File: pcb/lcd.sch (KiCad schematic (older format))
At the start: 1 part, among them J4 ITDB_TFT

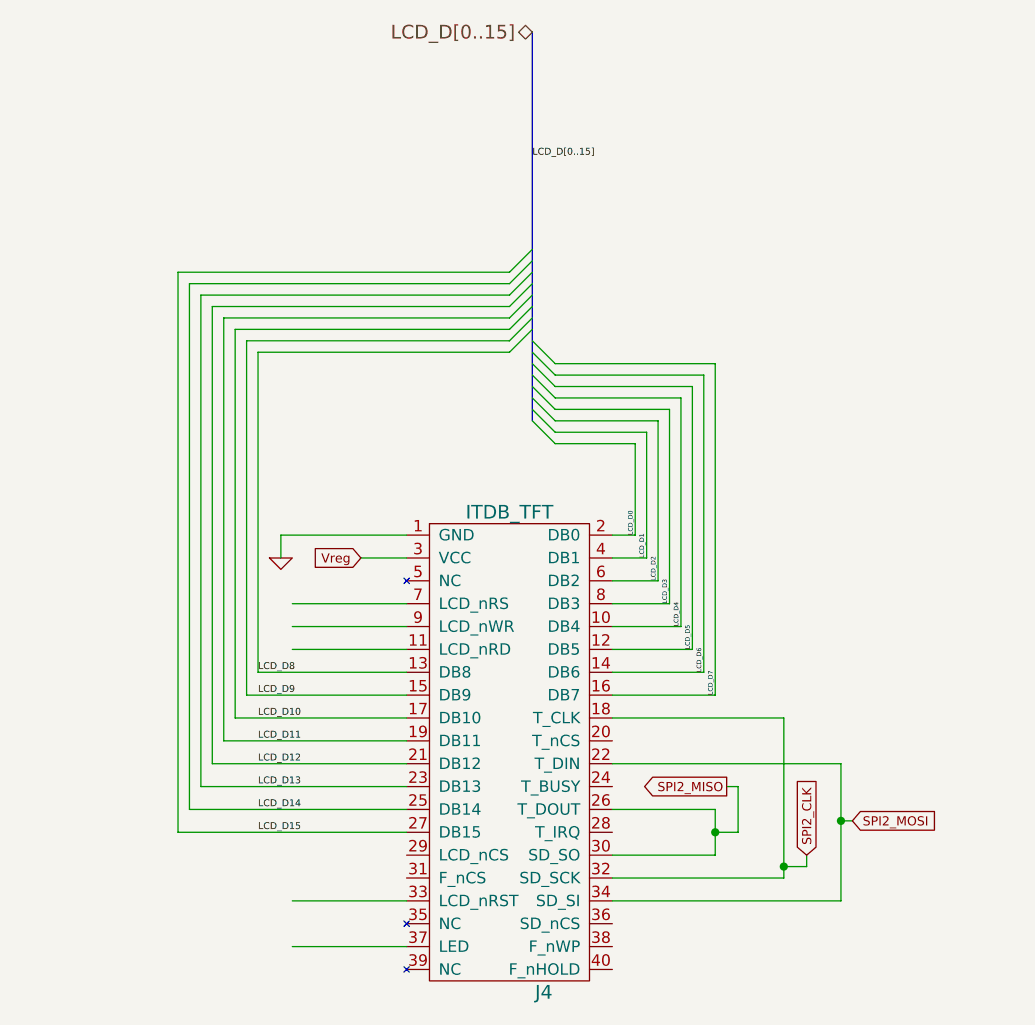
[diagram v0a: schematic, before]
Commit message: A few things: Remapped all interrupts and identified unusable pins on board Added all required connections for LCD and company Added pull-down resistor on STM32W Renamed some internal signals on RF for consistency
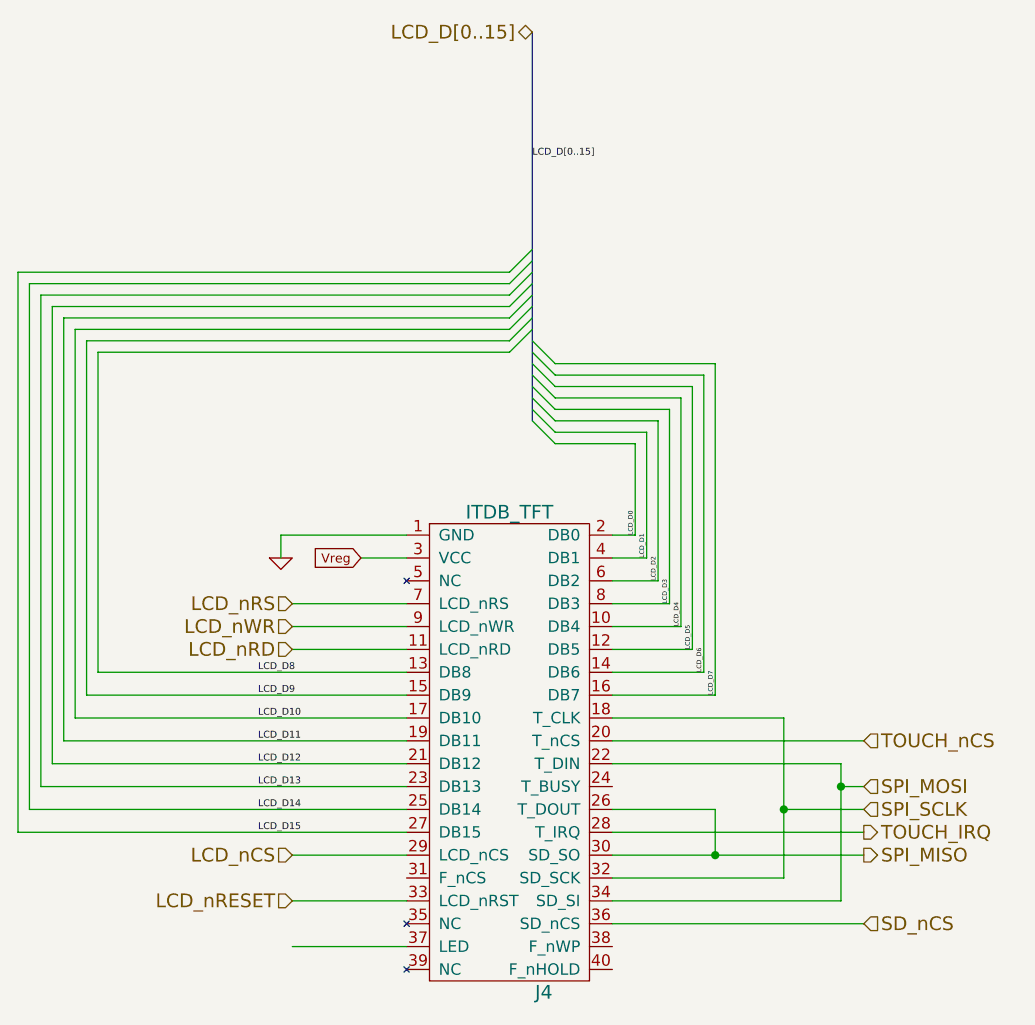
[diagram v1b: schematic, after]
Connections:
- net labels added: LCD_nCS, LCD_nRD, LCD_nRESET, LCD_nRS, LCD_nWR, SD_nCS, SPI_MISO, SPI_MOSI, SPI_SCLK, TOUCH_IRQ, TOUCH_nCS
- net labels removed: SPI2_CLK, SPI2_MISO, SPI2_MOSI
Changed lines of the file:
@@
-EESchema Schematic File Version 2  date 10/11/2012 11:52:24 AM
+EESchema Schematic File Version 2  date Sat 27 Oct 2012 09:22:30 PM EDT
 LIBS:power
 LIBS:device
@@
 $Descr A4 11700 8267
 encoding utf-8
-Sheet 5 7
+Sheet 2 7
 Title ""
-Date "11 oct 2012"
+Date "28 oct 2012"
 Rev ""
 Comp ""
@@
 Comment4 ""
 $EndDescr
+Wire Wire Line
+	6400 5100 5300 5100
+Wire Wire Line
+	6400 4700 5300 4700
+Wire Wire Line
+	6400 4600 6050 4600
+Wire Wire Line
+	4400 4800 3900 4800
+Wire Wire Line
+	4400 4300 2900 4300
+Wire Wire Line
+	4200 3500 4400 3500
+Wire Wire Line
+	3850 3500 3850 3400
+Wire Wire Line
+	3850 3400 4400 3400
+Wire Wire Line
+	5300 4400 6300 4400
+Wire Wire Line
+	5300 4600 5750 4600
+Wire Wire Line
+	5300 4200 6050 4200
+Wire Wire Line
+	5300 5000 6300 5000
+Wire Wire Line
+	5300 4900 6050 4900
+Wire Wire Line
+	4400 5000 3900 5000
+Wire Wire Line
+	4400 5200 3900 5200
+Wire Wire Line
+	4400 3900 3900 3900
+Wire Wire Line
+	4400 3800 3900 3800
+Wire Wire Line
+	4400 3700 3900 3700
+Wire Wire Line
+	5300 3400 5400 3400
+Wire Wire Line
+	5400 3400 5400 3000
+Wire Wire Line
+	5400 3000 5050 3000
+Wire Wire Line
+	5300 3500 5450 3500
+Wire Wire Line
+	5450 3500 5450 2950
+Wire Wire Line
+	5450 2950 5050 2950
+Wire Wire Line
+	5300 3600 5500 3600
+Wire Wire Line
+	5500 3600 5500 2900
+Wire Wire Line
+	5500 2900 5050 2900
+Wire Wire Line
+	5050 2850 5550 2850
+Wire Wire Line
+	5550 2850 5550 3700
+Wire Wire Line
+	5550 3700 5300 3700
+Wire Wire Line
+	5300 3800 5600 3800
+Wire Wire Line
+	5600 3800 5600 2800
+Wire Wire Line
+	5600 2800 5050 2800
+Wire Wire Line
+	5300 3900 5650 3900
+Wire Wire Line
+	5650 3900 5650 2750
+Wire Wire Line
+	5650 2750 5050 2750
+Wire Wire Line
+	5300 4000 5700 4000
+Wire Wire Line
+	5700 4000 5700 2700
+Wire Wire Line
+	5700 2700 5050 2700
+Wire Wire Line
+	5300 4100 5750 4100
+Wire Wire Line
+	5750 4100 5750 2650
+Wire Wire Line
+	5750 2650 5050 2650
+Wire Wire Line
+	4400 4000 3050 4000
+Wire Wire Line
+	3050 4000 3050 2600
+Wire Wire Line
+	3050 2600 4850 2600
+Wire Wire Line
+	4400 4100 3000 4100
+Wire Wire Line
+	3000 4100 3000 2550
+Wire Wire Line
+	3000 2550 4850 2550
+Wire Wire Line
+	4400 4200 2950 4200
+Wire Wire Line
+	2950 4200 2950 2500
+Wire Wire Line
+	2950 2500 4850 2500
+Wire Wire Line
+	2900 4300 2900 2450
+Wire Wire Line
+	2900 2450 4850 2450
+Wire Wire Line
+	4400 4400 2850 4400
+Wire Wire Line
+	2850 4400 2850 2400
+Wire Wire Line
+	2850 2400 4850 2400
+Wire Wire Line
+	4400 4500 2800 4500
+Wire Wire Line
+	2800 4500 2800 2350
+Wire Wire Line
+	2800 2350 4850 2350
+Wire Wire Line
+	4400 4600 2750 4600
+Wire Wire Line
+	2750 4600 2750 2300
+Wire Wire Line
+	2750 2300 4850 2300
+Wire Wire Line
+	4400 4700 2700 4700
+Wire Wire Line
+	2700 4700 2700 2250
+Wire Wire Line
+	2700 2250 4850 2250
+Wire Wire Line
+	6050 4900 6050 4200
+Connection ~ 6050 4600
+Wire Wire Line
+	5750 4600 5750 4800
+Wire Wire Line
+	6300 5000 6300 4400
+Connection ~ 6300 4500
 Wire Bus Line
-	4950 1200 4950 2900
-Wire Wire Line
-	5850 4500 5850 4700
-Wire Wire Line
-	5850 4500 5800 4500
-Connection ~ 6300 4650
-Wire Wire Line
-	6350 4650 6300 4650
-Wire Wire Line
-	6300 5000 6300 4400
-Wire Wire Line
-	6150 4800 6150 4850
-Connection ~ 5750 4700
-Wire Wire Line
-	5850 4700 5750 4700
-Wire Wire Line
-	5750 4800 5750 4600
-Connection ~ 6050 4850
-Wire Wire Line
-	6150 4850 6050 4850
-Wire Wire Line
-	6050 4900 6050 4200
-Wire Wire Line
-	4850 2250 3400 2250
-Wire Wire Line
-	3400 2250 3400 4700
-Wire Wire Line
-	3400 4700 4400 4700
-Wire Wire Line
-	4850 2300 3450 2300
-Wire Wire Line
-	3450 2300 3450 4600
-Wire Wire Line
-	3450 4600 4400 4600
-Wire Wire Line
-	4850 2350 3500 2350
-Wire Wire Line
-	3500 2350 3500 4500
-Wire Wire Line
-	3500 4500 4400 4500
-Wire Wire Line
-	4850 2400 3550 2400
-Wire Wire Line
-	3550 2400 3550 4400
-Wire Wire Line
-	3550 4400 4400 4400
-Wire Wire Line
-	4850 2450 3600 2450
-Wire Wire Line
-	3600 2450 3600 4300
-Wire Wire Line
-	4850 2500 3650 2500
-Wire Wire Line
-	3650 2500 3650 4200
-Wire Wire Line
-	3650 4200 4400 4200
-Wire Wire Line
-	4850 2550 3700 2550
-Wire Wire Line
-	3700 2550 3700 4100
-Wire Wire Line
-	3700 4100 4400 4100
-Wire Wire Line
-	4850 2600 3750 2600
-Wire Wire Line
-	3750 2600 3750 4000
-Wire Wire Line
-	3750 4000 4400 4000
-Wire Wire Line
-	5050 2650 5750 2650
-Wire Wire Line
-	5750 2650 5750 4100
-Wire Wire Line
-	5750 4100 5300 4100
-Wire Wire Line
-	5050 2700 5700 2700
-Wire Wire Line
-	5700 2700 5700 4000
-Wire Wire Line
-	5700 4000 5300 4000
-Wire Wire Line
-	5050 2750 5650 2750
-Wire Wire Line
-	5650 2750 5650 3900
-Wire Wire Line
-	5650 3900 5300 3900
-Wire Wire Line
-	5050 2800 5600 2800
-Wire Wire Line
-	5600 2800 5600 3800
-Wire Wire Line
-	5600 3800 5300 3800
-Wire Wire Line
-	5300 3700 5550 3700
-Wire Wire Line
-	5550 3700 5550 2850
-Wire Wire Line
-	5550 2850 5050 2850
-Wire Wire Line
-	5050 2900 5500 2900
-Wire Wire Line
-	5500 2900 5500 3600
-Wire Wire Line
-	5500 3600 5300 3600
-Wire Wire Line
-	5050 2950 5450 2950
-Wire Wire Line
-	5450 2950 5450 3500
-Wire Wire Line
-	5450 3500 5300 3500
-Wire Wire Line
-	5050 3000 5400 3000
-Wire Wire Line
-	5400 3000 5400 3400
-Wire Wire Line
-	5400 3400 5300 3400
-Wire Wire Line
-	4400 3700 3900 3700
-Wire Wire Line
-	4400 3800 3900 3800
-Wire Wire Line
-	4400 3900 3900 3900
-Wire Wire Line
-	4400 5200 3900 5200
-Wire Wire Line
-	4400 5000 3900 5000
-Wire Wire Line
-	5750 4800 5300 4800
-Wire Wire Line
-	6050 4900 5300 4900
-Wire Wire Line
-	6300 5000 5300 5000
-Wire Wire Line
-	6050 4200 5300 4200
-Wire Wire Line
-	5750 4600 5300 4600
-Wire Wire Line
-	6300 4400 5300 4400
-Wire Wire Line
-	4400 3400 3850 3400
-Wire Wire Line
-	3850 3400 3850 3500
-Wire Wire Line
-	4200 3500 4400 3500
-Wire Wire Line
-	3600 4300 4400 4300
+	4950 2900 4950 1200
+Wire Wire Line
+	6400 4500 6300 4500
+Wire Wire Line
+	5300 4800 6400 4800
+Connection ~ 5750 4800
+Wire Wire Line
+	6400 4300 5300 4300
+Text HLabel 6400 5100 2    60   Input ~ 0
+SD_nCS
+Text HLabel 6400 4300 2    60   Input ~ 0
+TOUCH_nCS
+Text HLabel 3900 5000 0    60   Input ~ 0
+LCD_nRESET
+Text HLabel 6400 4600 2    60   Input ~ 0
+SPI_SCLK
+Text HLabel 6400 4500 2    60   Input ~ 0
+SPI_MOSI
+Text HLabel 6400 4800 2    60   Output ~ 0
+SPI_MISO
+Text HLabel 3900 4800 0    60   Input ~ 0
+LCD_nCS
+Text HLabel 3900 3900 0    60   Input ~ 0
+LCD_nRD
+Text HLabel 3900 3800 0    60   Input ~ 0
+LCD_nWR
+Text HLabel 3900 3700 0    60   Input ~ 0
+LCD_nRS
+Text HLabel 6400 4700 2    60   Output ~ 0
+TOUCH_IRQ
 Text Label 4950 1750 0    30   ~ 0
 LCD_D[0..15]
@@
 Text HLabel 4950 1200 0    60   BiDi ~ 0
 LCD_D[0..15]
-Text GLabel 6350 4650 2    40   Input ~ 0
-SPI2_MOSI
-Text GLabel 5800 4500 0    40   Output ~ 0
-SPI2_MISO
-Text GLabel 6150 4800 1    40   Input ~ 0
-SPI2_CLK
 Entry Wire Line
 	4850 2250 4950 2150

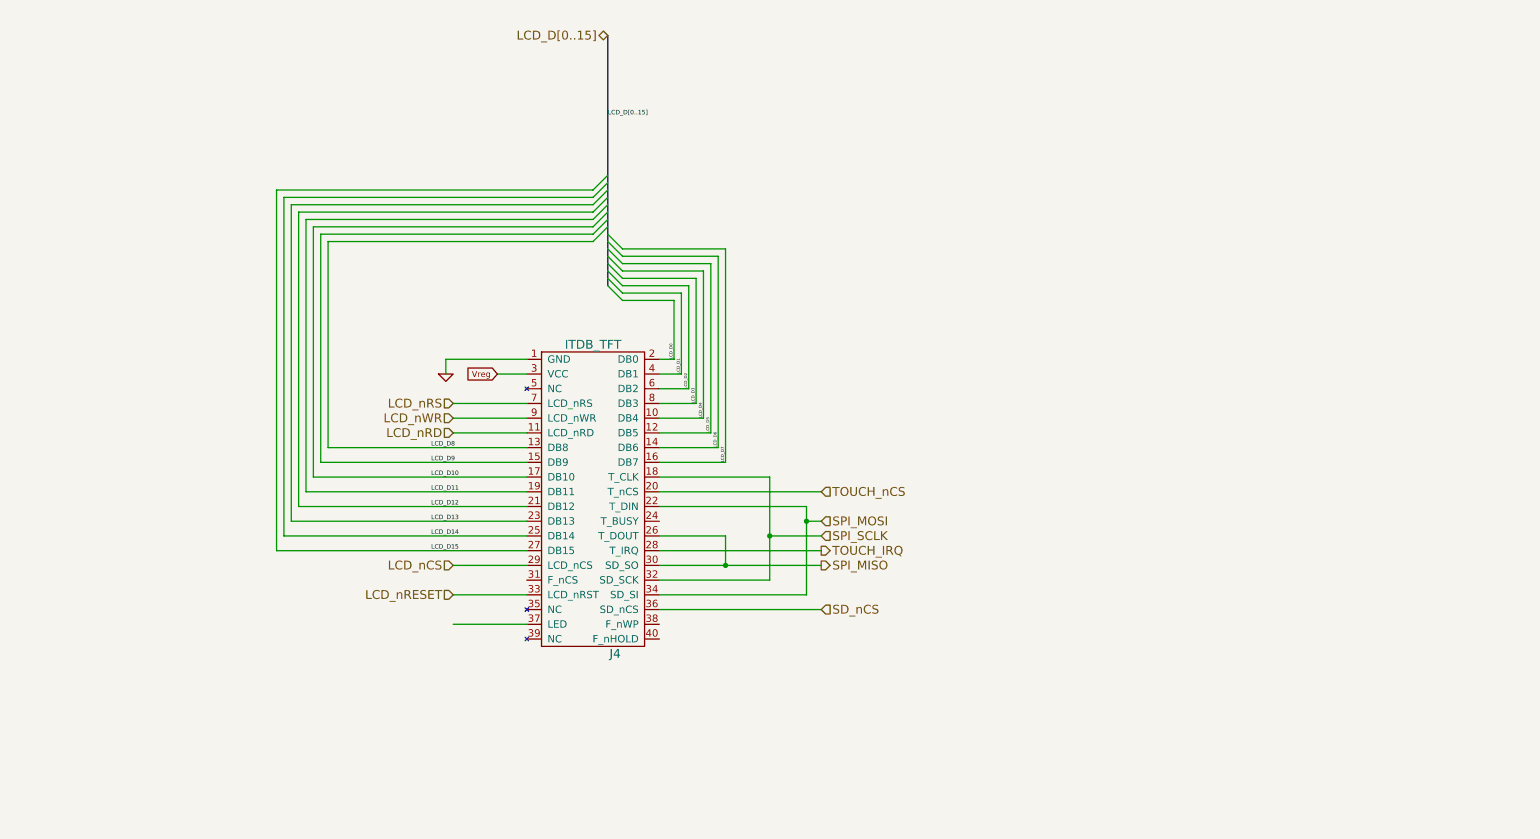
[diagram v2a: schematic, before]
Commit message: Changed some values and connected more LCD signals
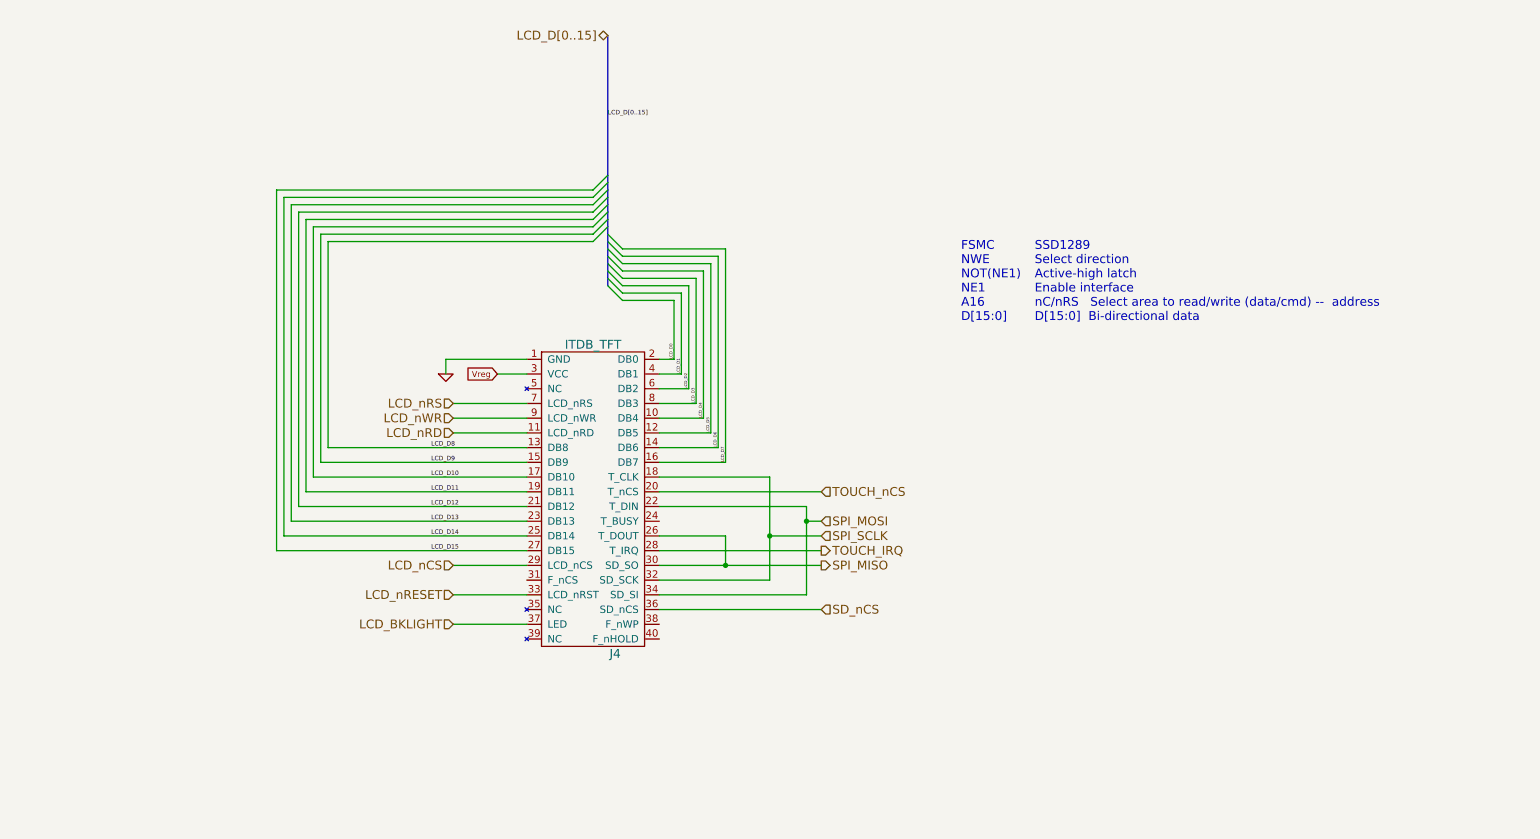
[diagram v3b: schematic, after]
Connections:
- net LCD_BKLIGHT: now reaches J4.37 (LED)
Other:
- note added: "FSMC\nNWE\nNOT(NE1)\nNE1\nA16\nD[15:0]\n"
- note added: "SSD1289\nSelect direction\nActive-high latch\nEnable interface\nnC/nRS Select area to read/write (data/cmd) -- address\nD[15:0] Bi-directional data\n"
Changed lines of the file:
@@
-EESchema Schematic File Version 2  date Sun 28 Oct 2012 01:53:13 PM EDT
+EESchema Schematic File Version 2  date Sun 28 Oct 2012 06:31:28 PM EDT
 LIBS:power
 LIBS:device
@@
 Comment4 ""
 $EndDescr
+Text HLabel 3900 5200 0    60   Input ~ 0
+LCD_BKLIGHT
+Text Notes 7850 3150 0    60   ~ 0
+SSD1289\nSelect direction\nActive-high latch\nEnable interface\nnC/nRS   Select area to read/write (data/cmd) --  address\nD[15:0]  Bi-directional data\n
+Text Notes 7350 3150 0    60   ~ 0
+FSMC\nNWE\nNOT(NE1)\nNE1\nA16\nD[15:0]\n
 Wire Wire Line
 	6400 5100 5300 5100
@@
 	2700 2250 4850 2250
 Wire Wire Line
-	6050 4900 6050 4200
+	6050 4900 6050 4600
+Wire Wire Line
+	6050 4600 6050 4200
 Connection ~ 6050 4600
 Wire Wire Line
 	5750 4600 5750 4800
 Wire Wire Line
-	6300 5000 6300 4400
+	6300 5000 6300 4500
+Wire Wire Line
+	6300 4500 6300 4400
 Connection ~ 6300 4500
 Wire Bus Line
-	4950 2900 4950 1200
+	4950 2900 4950 2850
+Wire Bus Line
+	4950 2850 4950 2800
+Wire Bus Line
+	4950 2800 4950 2750
+Wire Bus Line
+	4950 2750 4950 2700
+Wire Bus Line
+	4950 2700 4950 2650
+Wire Bus Line
+	4950 2650 4950 2600
+Wire Bus Line
+	4950 2600 4950 2550
+Wire Bus Line
+	4950 2550 4950 2500
+Wire Bus Line
+	4950 2500 4950 2450
+Wire Bus Line
+	4950 2450 4950 2400
+Wire Bus Line
+	4950 2400 4950 2350
+Wire Bus Line
+	4950 2350 4950 2300
+Wire Bus Line
+	4950 2300 4950 2250
+Wire Bus Line
+	4950 2250 4950 2200
+Wire Bus Line
+	4950 2200 4950 2150
+Wire Bus Line
+	4950 2150 4950 1200
 Wire Wire Line
 	6400 4500 6300 4500
 Wire Wire Line
-	5300 4800 6400 4800
+	5300 4800 5750 4800
+Wire Wire Line
+	5750 4800 6400 4800
 Connection ~ 5750 4800
 Wire Wire Line

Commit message: Put the SC4541 setup in the LCD sheet in buck topology.
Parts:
- added C? (x2): 1u, symbol CAP
- added L?: CVH252009-4R7MCT-ND, symbol INDUCTOR
- added R?: 10, symbol RES
- added R?: 220k, symbol RES
- added U1: SC4541, symbol SC4541
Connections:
- net labels added: LED_EN, LED_PWM, Vbat
- net labels removed: LCD_BKLIGHT
- wire segments 74 -> 89
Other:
- note added: "LED Backlight PWM Controller"
- moved on the sheet: J4

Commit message: Revert "Put the SC4541 setup in the LCD sheet in buck topology."
This reverts commit 49a1ec046560eed971b78a640ae727a0fcab9c9b.
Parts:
- removed C? (x2): 1u, symbol CAP
- removed L?: CVH252009-4R7MCT-ND, symbol INDUCTOR
- removed R?: 10, symbol RES
- removed R?: 220k, symbol RES
- removed U1: SC4541, symbol SC4541
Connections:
- net labels added: LCD_BKLIGHT
- net labels removed: LED_EN, LED_PWM, Vbat
- wire segments 89 -> 74
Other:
- note removed: "LED Backlight PWM Controller"
- moved on the sheet: J4
